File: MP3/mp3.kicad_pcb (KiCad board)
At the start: 2 copper layers, 18.3 x 51.5 mm, 38 parts, among them J1 USB4105-GF-A, J2 LEFT, J3 DEBUG, J4 RIGHT, U1 W25Q128JV, U2 RP2040, U3 MCP1702T-3302E_CB, Y1 12MHz

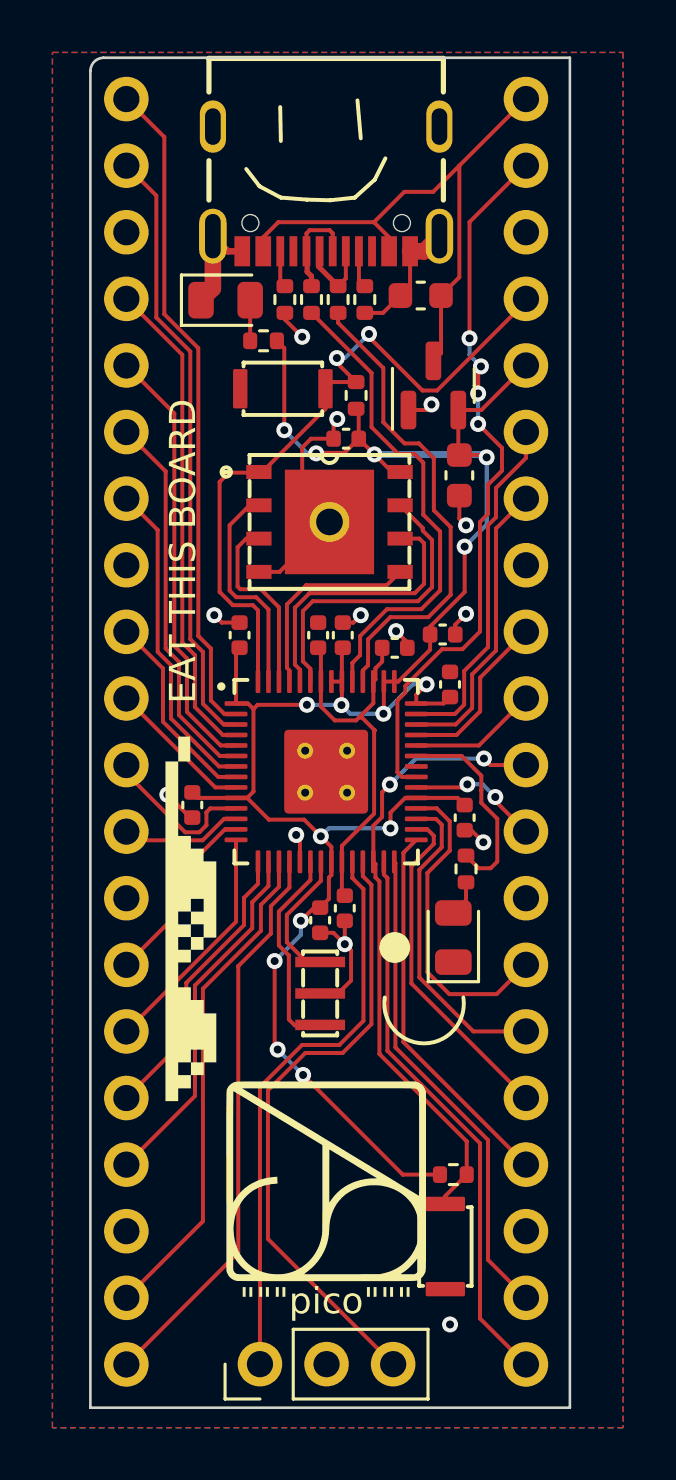
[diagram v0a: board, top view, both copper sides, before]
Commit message: round corners, move termination resistors close to rp2040
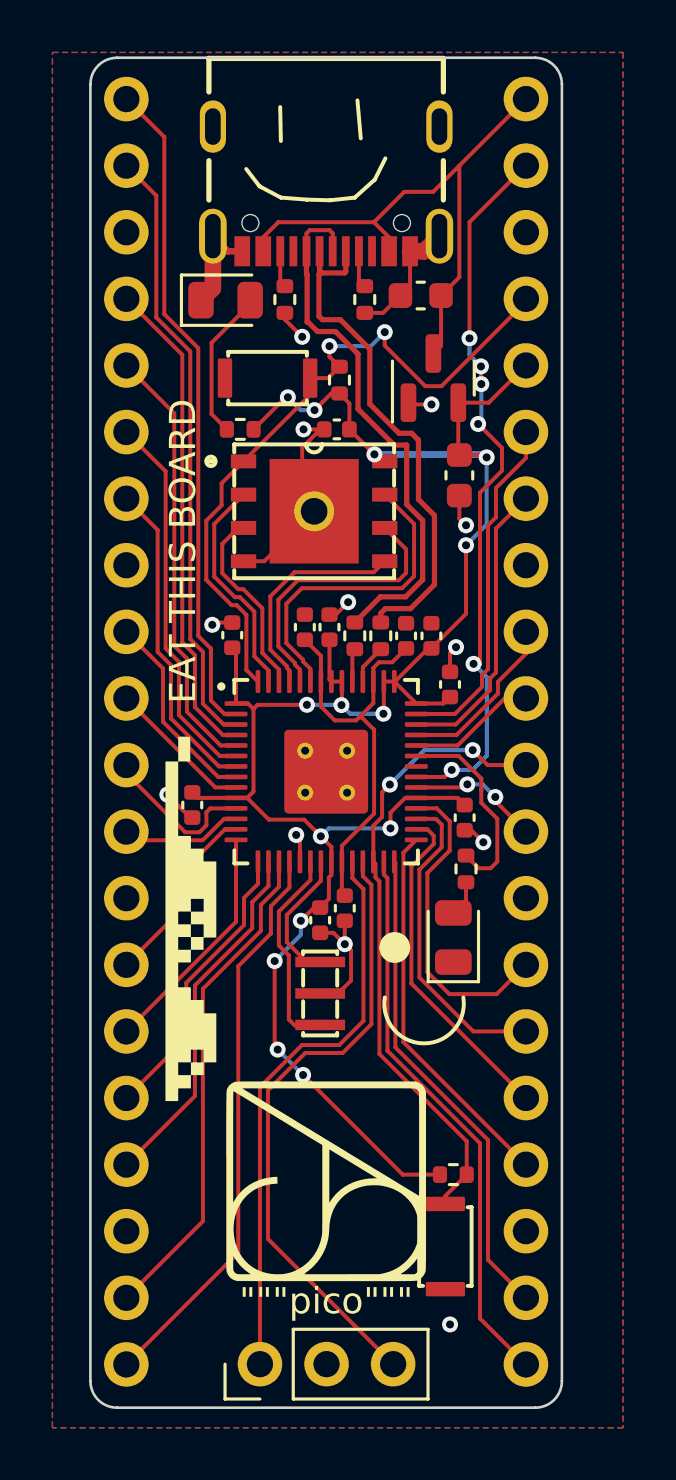
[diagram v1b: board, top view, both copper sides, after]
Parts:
- moved R6 12.9 mm to (116.9, 93.2)
- moved R5 12.9 mm to (117.9, 93.2)
- moved R8 3.49 mm to (112.5, 85.4)
- moved R3 0.86 mm to (116.3, 83.5)
- moved U1 0.71 mm to (115.4, 88.5)
- moved S2 0.71 mm to (113.6, 83.4)
- moved C9 0.63 mm to (118.9, 93.2), turned to 90 degrees
- moved C7 0.59 mm to (116.0, 92.9)
- moved C11 0.59 mm to (115.0, 92.9)
- moved C1 0.50 mm to (116.2, 85.4)
- moved C8 0.43 mm to (119.8, 93.2), turned to 90 degrees
- moved C2 0.28 mm to (112.2, 93.2)
- moved U3 0.28 mm to (119.9, 83.4)
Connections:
- J1 pad A6: Net-(J1-PadA6) -> /D+
- J1 pad A7: Net-(J1-PadA7) -> /D-
- J1 pad B6: Net-(J1-PadA6) -> /D+
- J1 pad B7: Net-(J1-PadA7) -> /D-
- R5 pad 1: Net-(J1-PadA7) -> /D-
- R5 pad 2: /D- -> Net-(R5-Pad2)
- R6 pad 1: Net-(J1-PadA6) -> /D+
- R6 pad 2: /D+ -> Net-(R6-Pad2)
- U2 pad 46: /D- -> Net-(R5-Pad2)
- U2 pad 47: /D+ -> Net-(R6-Pad2)
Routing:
- net Net-(D2-Pad2): track 1.55 -> 5.78 mm
- net +3V3: track 80.7 -> 76.7 mm, vias 15 -> 14
- net Net-(J1-PadA6): track 3.87 -> 0.00 mm
- net Net-(J1-PadA7): track 3.10 -> 0.00 mm
- net /D-: track 18.4 -> 20.7 mm
- net /D+: track 18.6 -> 20.8 mm
- net GND: track 32.9 -> 31.1 mm, vias 13 -> 12
- net Net-(R5-Pad2): track 0.00 -> 1.52 mm
- net Net-(R6-Pad2): track 0.00 -> 1.27 mm
- net Net-(C10-Pad1): track 14.7 -> 15.8 mm
- net Net-(U1-Pad5): track 7.81 -> 8.47 mm
- net /GPIO23: track 27.5 -> 27.8 mm, vias 4 -> 6
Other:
- board size 18.3 x 51.5 mm -> 18 x 51.5 mm

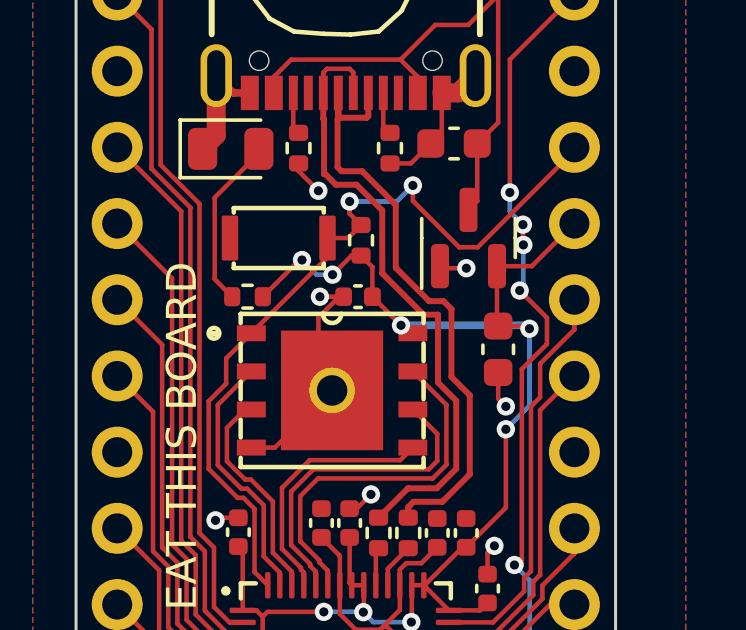
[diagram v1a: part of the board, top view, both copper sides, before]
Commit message: fix via too close to memory 3.3v pad
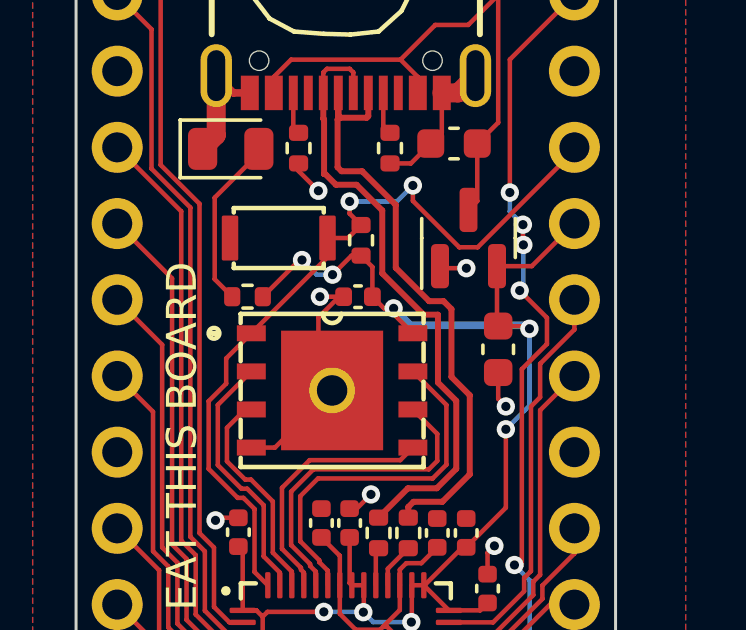
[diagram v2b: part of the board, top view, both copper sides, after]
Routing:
- net +3V3: track 76.7 -> 77.3 mm
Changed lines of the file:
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@@
   (segment (start 115.6208 100.8888) (end 114.9858 100.2538) (width 0.1524) (layer "F.Cu") (net 2))
   (segment (start 121.8562 86.347) (end 121.9454 86.4362) (width 0.1524) (layer "F.Cu") (net 2))
-  (segment (start 117.9296 86.5886) (end 117.6642 86.3232) (width 0.1524) (layer "F.Cu") (net 2))
   (segment (start 120.1654 113.792) (end 118.745 113.792) (width 0.1524) (layer "F.Cu") (net 2))
   (segment (start 113.212677 95.874523) (end 113.0526 96.0346) (width 0.1524) (layer "F.Cu") (net 2))
@@
   (segment (start 112.3865 95.825) (end 112.3865 93.8419) (width 0.1524) (layer "F.Cu") (net 2))
   (segment (start 115.951 93.3932) (end 115.951 94.9145) (width 0.1524) (layer "F.Cu") (net 2))
-  (segment (start 118.0592 86.5886) (end 117.9296 86.5886) (width 0.1524) (layer "F.Cu") (net 2))
   (segment (start 119.7128 93.7234) (end 118.4487 94.9875) (width 0.1524) (layer "F.Cu") (net 2))
   (segment (start 115.5954 103.6092) (end 115.359518 103.6092) (width 0.1524) (layer "F.Cu") (net 2))
   (segment (start 116.7104 85.3694) (end 116.7104 84.3782) (width 0.1524) (layer "F.Cu") (net 2))
   (segment (start 113.639729 100.2538) (end 112.810929 99.425) (width 0.1524) (layer "F.Cu") (net 2))
+  (segment (start 117.098047 85.757047) (end 116.7104 85.3694) (width 0.1524) (layer "F.Cu") (net 2))
   (segment (start 119.8372 93.7234) (end 119.7128 93.7234) (width 0.1524) (layer "F.Cu") (net 2))
   (segment (start 116.424 95.8692) (end 116.424 94.9875) (width 0.1524) (layer "F.Cu") (net 2))
@@
   (segment (start 114.363512 84.145852) (end 114.280948 84.145852) (width 0.1524) (layer "F.Cu") (net 2))
   (segment (start 120.8634 86.3064) (end 120.904 86.347) (width 0.1524) (layer "F.Cu") (net 2))
+  (segment (start 117.417553 85.946953) (end 118.0592 86.5886) (width 0.1524) (layer "F.Cu") (net 2))
   (segment (start 116.7104 84.3782) (end 116.332 83.9998) (width 0.1524) (layer "F.Cu") (net 2))
   (segment (start 118.024 94.9875) (end 118.424 94.9875) (width 0.1524) (layer "F.Cu") (net 2))
   (segment (start 113.0526 96.0346) (end 112.843 95.825) (width 0.1524) (layer "F.Cu") (net 2))
+  (segment (start 117.417553 85.757047) (end 117.417553 85.946953) (width 0.1524) (layer "F.Cu") (net 2))
   (segment (start 120.8634 84.3511) (end 120.8634 86.3064) (width 0.1524) (layer "F.Cu") (net 2))
   (segment (start 118.024 96.2001) (end 118.024 94.9875) (width 0.1524) (layer "F.Cu") (net 2))
@@
   (segment (start 115.9288 103.2758) (end 115.9288 102.461148) (width 0.1524) (layer "F.Cu") (net 2))
   (segment (start 116.024 102.365948) (end 115.9288 102.461148) (width 0.1524) (layer "F.Cu") (net 2))
+  (segment (start 117.417553 85.757047) (end 117.098047 85.757047) (width 0.1524) (layer "F.Cu") (net 2))
   (segment (start 121.1585 92.4021) (end 119.8372 93.7234) (width 0.1524) (layer "F.Cu") (net 2))
-  (segment (start 117.6642 86.3232) (end 116.7104 85.3694) (width 0.1524) (layer "F.Cu") (net 2))
   (segment (start 113.860056 105.646744) (end 113.860056 108.907056) (width 0.1524) (layer "F.Cu") (net 2))
   (segment (start 119.2615 95.825) (end 120.301 95.825) (width 0.1524) (layer "F.Cu") (net 2))
@@
   (segment (start 121.1072 99.6976) (end 120.8346 99.425) (width 0.1524) (layer "F.Cu") (net 2))
   (segment (start 118.745 113.792) (end 114.944514 109.991514) (width 0.1524) (layer "F.Cu") (net 2))
-  (via (at 117.6642 86.3232) (size 0.6096) (drill 0.3048) (layers "F.Cu" "B.Cu") (net 2))
+  (via (at 117.417553 85.757047) (size 0.6096) (drill 0.3048) (layers "F.Cu" "B.Cu") (net 2))
   (via (at 121.1585 89.788502) (size 0.6096) (drill 0.3048) (layers "F.Cu" "B.Cu") (net 2))
   (via (at 114.8583 104.110418) (size 0.6096) (drill 0.3048) (layers "F.Cu" "B.Cu") (net 2))
@@
   (via (at 116.4082 95.885) (size 0.6096) (drill 0.3048) (layers "F.Cu" "B.Cu") (net 2))
   (via (at 115.381568 84.635068) (size 0.6096) (drill 0.3048) (layers "F.Cu" "B.Cu") (net 2))
-  (segment (start 117.6642 86.3232) (end 121.8324 86.3232) (width 0.254) (layer "B.Cu") (net 2))
+  (segment (start 121.8324 86.3232) (end 121.9454 86.4362) (width 0.254) (layer "B.Cu") (net 2))
   (segment (start 116.4082 95.885) (end 116.397723 95.874523) (width 0.1524) (layer "B.Cu") (net 2))
+  (segment (start 117.417553 85.757047) (end 117.983706 86.3232) (width 0.254) (layer "B.Cu") (net 2))
   (segment (start 114.8583 104.110418) (end 114.8583 104.6485) (width 0.1524) (layer "B.Cu") (net 2))
   (segment (start 121.9454 89.001602) (end 121.9454 86.4362) (width 0.1524) (layer "B.Cu") (net 2))
@@
   (segment (start 114.852728 84.635068) (end 115.381568 84.635068) (width 0.1524) (layer "B.Cu") (net 2))
   (segment (start 118.0089 96.2152) (end 116.7384 96.2152) (width 0.1524) (layer "B.Cu") (net 2))
-  (segment (start 121.8324 86.3232) (end 121.9454 86.4362) (width 0.254) (layer "B.Cu") (net 2))
+  (segment (start 117.983706 86.3232) (end 121.8324 86.3232) (width 0.254) (layer "B.Cu") (net 2))
   (segment (start 116.397723 95.874523) (end 115.0911 95.874523) (width 0.1524) (layer "B.Cu") (net 2))
   (segment (start 114.8583 104.6485) (end 113.860056 105.646744) (width 0.1524) (layer "B.Cu") (net 2))
